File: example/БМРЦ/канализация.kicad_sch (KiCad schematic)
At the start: 0 parts

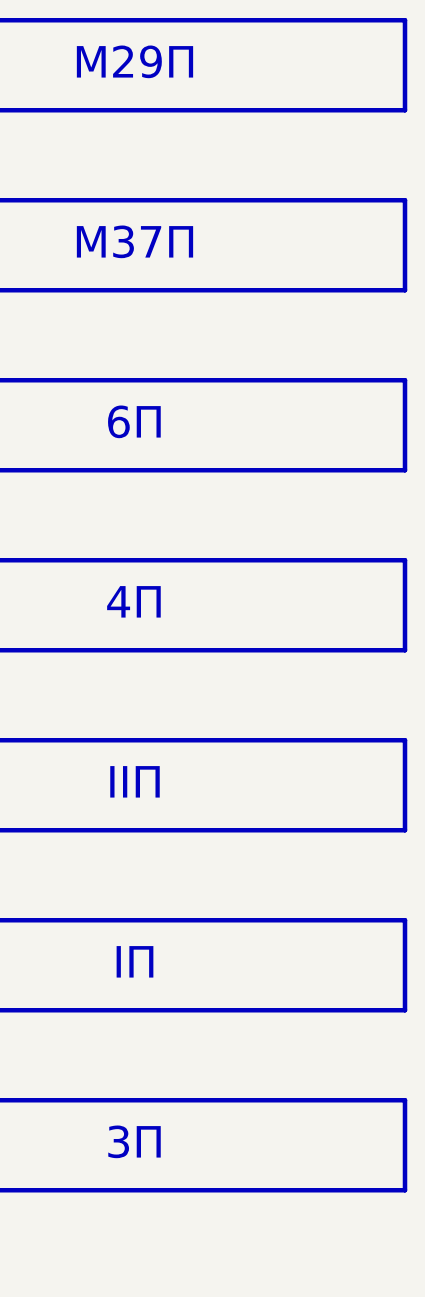
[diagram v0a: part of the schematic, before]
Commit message: В двухнитке ЭЦ проложен кабель СЦБ
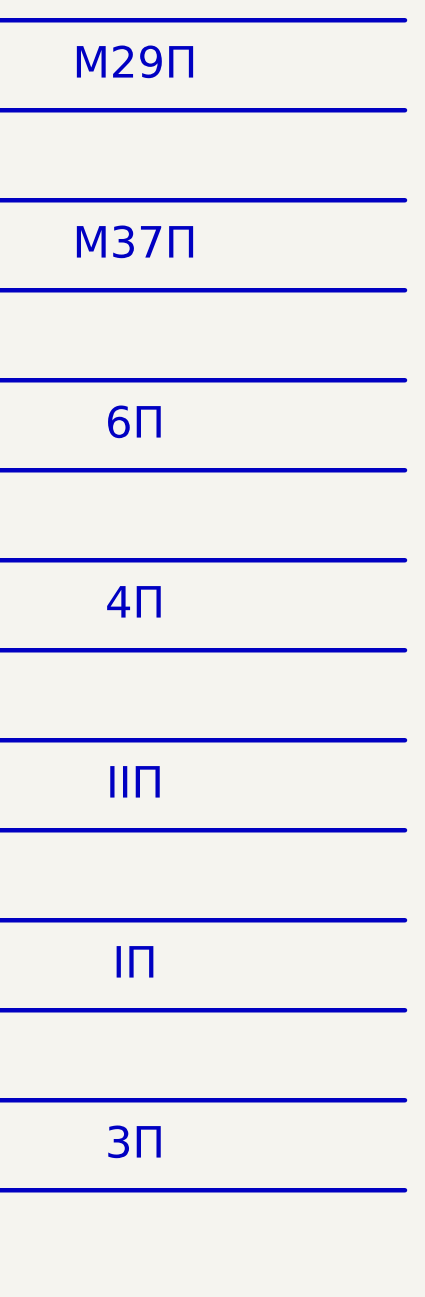
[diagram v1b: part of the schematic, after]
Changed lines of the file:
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@@
-	(polyline
-		(pts
-			(xy 390 150) (xy 390 160)
-		)
-		(stroke
-			(width 0.5)
-			(type default)
-		)
-	)
 	(polyline
 		(pts
@@
 	(polyline
 		(pts
-			(xy 390 70) (xy 390 80)
-		)
-		(stroke
-			(width 0.5)
-			(type default)
-		)
-	)
-	(polyline
-		(pts
 			(xy 75 200) (xy 95 200)
 		)
@@
 	(polyline
 		(pts
-			(xy 390 170) (xy 390 180)
-		)
-		(stroke
-			(width 0.5)
-			(type default)
-		)
-	)
-	(polyline
-		(pts
 			(xy 190 150) (xy 186 146)
 		)
@@
 	(polyline
 		(pts
-			(xy 390 190) (xy 390 200)
-		)
-		(stroke
-			(width 0.5)
-			(type default)
-		)
-	)
-	(polyline
-		(pts
 			(xy 210 150) (xy 210 160)
 		)
@@
 	(polyline
 		(pts
-			(xy 390 130) (xy 390 140)
-		)
-		(stroke
-			(width 0.5)
-			(type default)
-		)
-	)
-	(polyline
-		(pts
 			(xy 320 90) (xy 390 90)
 		)
@@
 	(polyline
 		(pts
-			(xy 390 110) (xy 390 120)
-		)
-		(stroke
-			(width 0.5)
-			(type default)
-		)
-	)
-	(polyline
-		(pts
 			(xy 80 140) (xy 140 140)
 		)
@@
 		)
 		(stroke
-			(width 0.5)
-			(type default)
-		)
-	)
-	(polyline
-		(pts
-			(xy 390 90) (xy 390 100)
-		)
-		(stroke

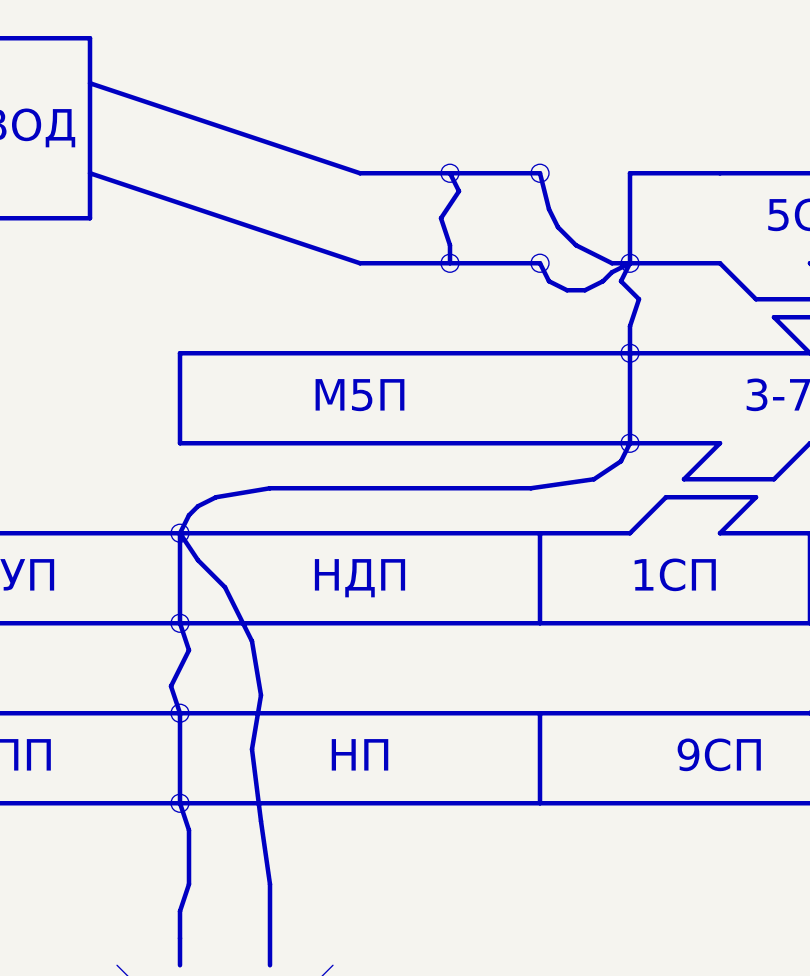
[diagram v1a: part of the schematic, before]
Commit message: Упрощены УГО ДТ для фазочувствительных РЦ, скрыты точки для двойных СС
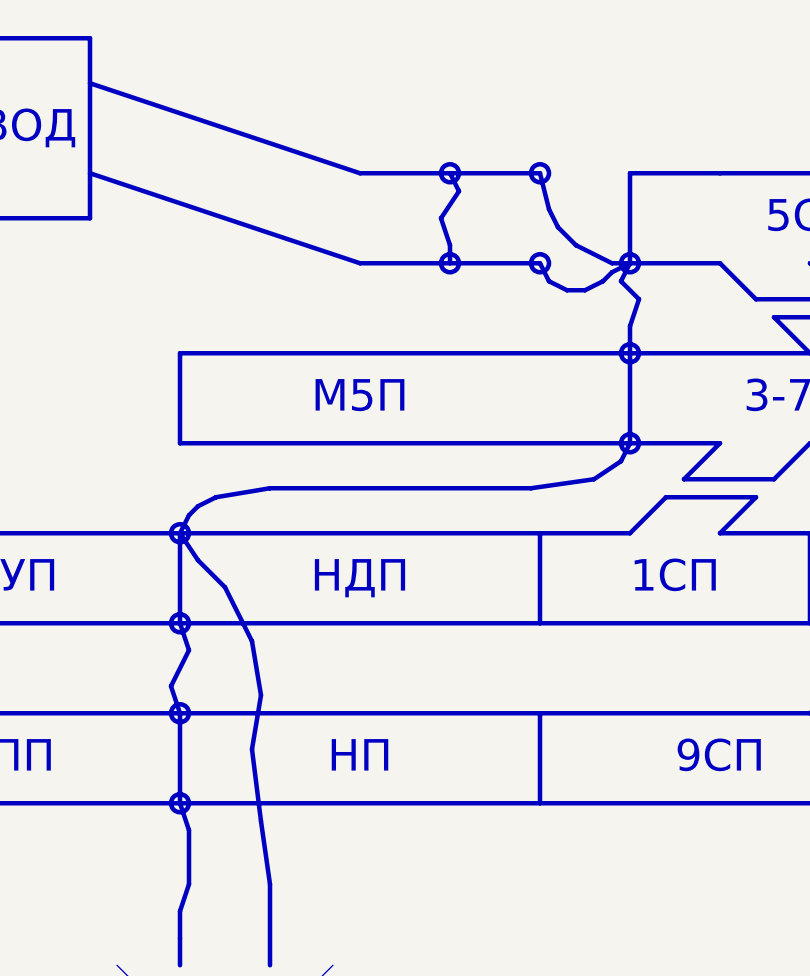
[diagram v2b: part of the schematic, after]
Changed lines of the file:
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@@
 		(radius 1)
 		(stroke
-			(width 0)
+			(width 0.5)
 			(type default)
 		)
 		(fill
 			(type color)
-			(color 0 0 0 1)
+			(color 0 0 194 1)
 		)
 	)
@@
 		(radius 1)
 		(stroke
-			(width 0)
-			(type default)
+			(width 0.5)
+			(type dash_dot_dot)
 		)
 		(fill
 			(type color)
-			(color 0 0 0 1)
+			(color 0 0 194 1)
 		)
 	)
@@
 		(radius 1)
 		(stroke
-			(width 0)
+			(width 0.5)
 			(type default)
 		)
 		(fill
 			(type color)
-			(color 0 0 0 1)
+			(color 0 0 194 1)
 		)
 	)
@@
 		(radius 1)
 		(stroke
-			(width 0)
-			(type default)
+			(width 0.5)
+			(type dash_dot_dot)
 		)
 		(fill
 			(type color)
-			(color 0 0 0 1)
+			(color 0 0 194 1)
 		)
 	)
@@
 		(radius 1)
 		(stroke
-			(width 0)
-			(type default)
+			(width 0.5)
+			(type dash_dot_dot)
 		)
 		(fill
 			(type color)
-			(color 0 0 0 1)
+			(color 0 0 194 1)
 		)
 	)
@@
 		(radius 1)
 		(stroke
-			(width 0)
-			(type default)
+			(width 0.5)
+			(type dash_dot_dot)
 		)
 		(fill
 			(type color)
-			(color 0 0 0 1)
+			(color 0 0 194 1)
 		)
 	)
@@
 		(radius 1)
 		(stroke
-			(width 0)
-			(type default)
+			(width 0.5)
+			(type dash_dot_dot)
 		)
 		(fill
 			(type color)
-			(color 0 0 0 1)
+			(color 0 0 194 1)
 		)
 	)
@@
 		(radius 1)
 		(stroke
-			(width 0)
+			(width 0.5)
 			(type default)
 		)
 		(fill
 			(type color)
-			(color 0 0 0 1)
+			(color 0 0 194 1)
 		)
 	)
@@
 		(radius 1)
 		(stroke
-			(width 0)
-			(type default)
+			(width 0.5)
+			(type dash_dot_dot)
 		)
 		(fill
 			(type color)
-			(color 0 0 0 1)
+			(color 0 0 194 1)
 		)
 	)
@@
 		(radius 1)
 		(stroke
-			(width 0)
+			(width 0.5)
 			(type default)
 		)
 		(fill
 			(type color)
-			(color 0 0 0 1)
+			(color 0 0 194 1)
 		)
 	)
@@
 		(radius 1)
 		(stroke
-			(width 0)
-			(type default)
+			(width 0.5)
+			(type dash_dot_dot)
 		)
 		(fill
 			(type color)
-			(color 0 0 0 1)
+			(color 0 0 194 1)
 		)
 	)
